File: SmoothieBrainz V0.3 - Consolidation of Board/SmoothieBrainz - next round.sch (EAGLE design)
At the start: 153 parts, among them IC1 LPC1769, IC5 LD117ADT33TR, Q1 BSL207SP, Q2 12MHz, SW1 SW_TACT_4P_B, SW3 SW_TACT_4P_B, U2 HC_05, U3 USD-SOCKETUSD, X1 GMSTBV2, X14 USBPTH, X2 MSTBA2, X3 MSTBA4

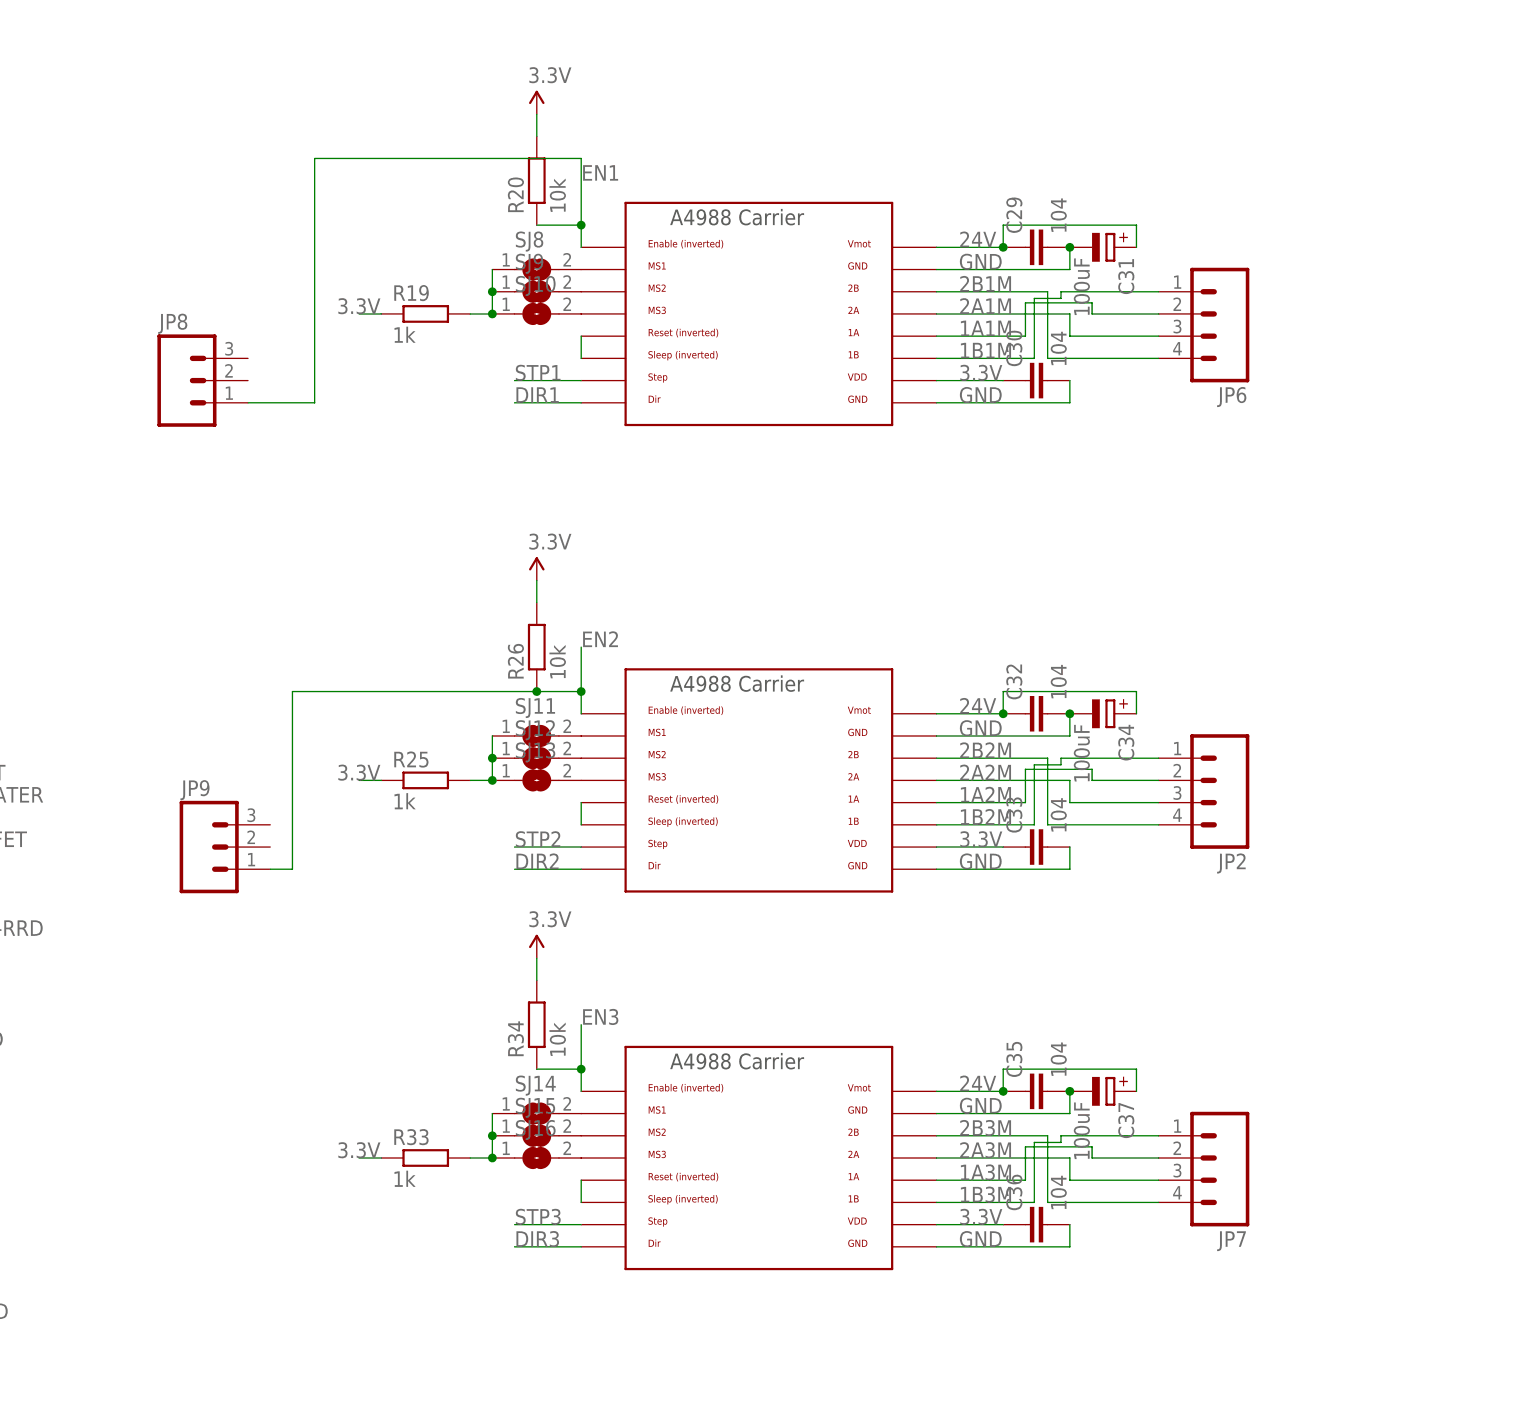
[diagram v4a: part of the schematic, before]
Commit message: about to revert y stepper layout
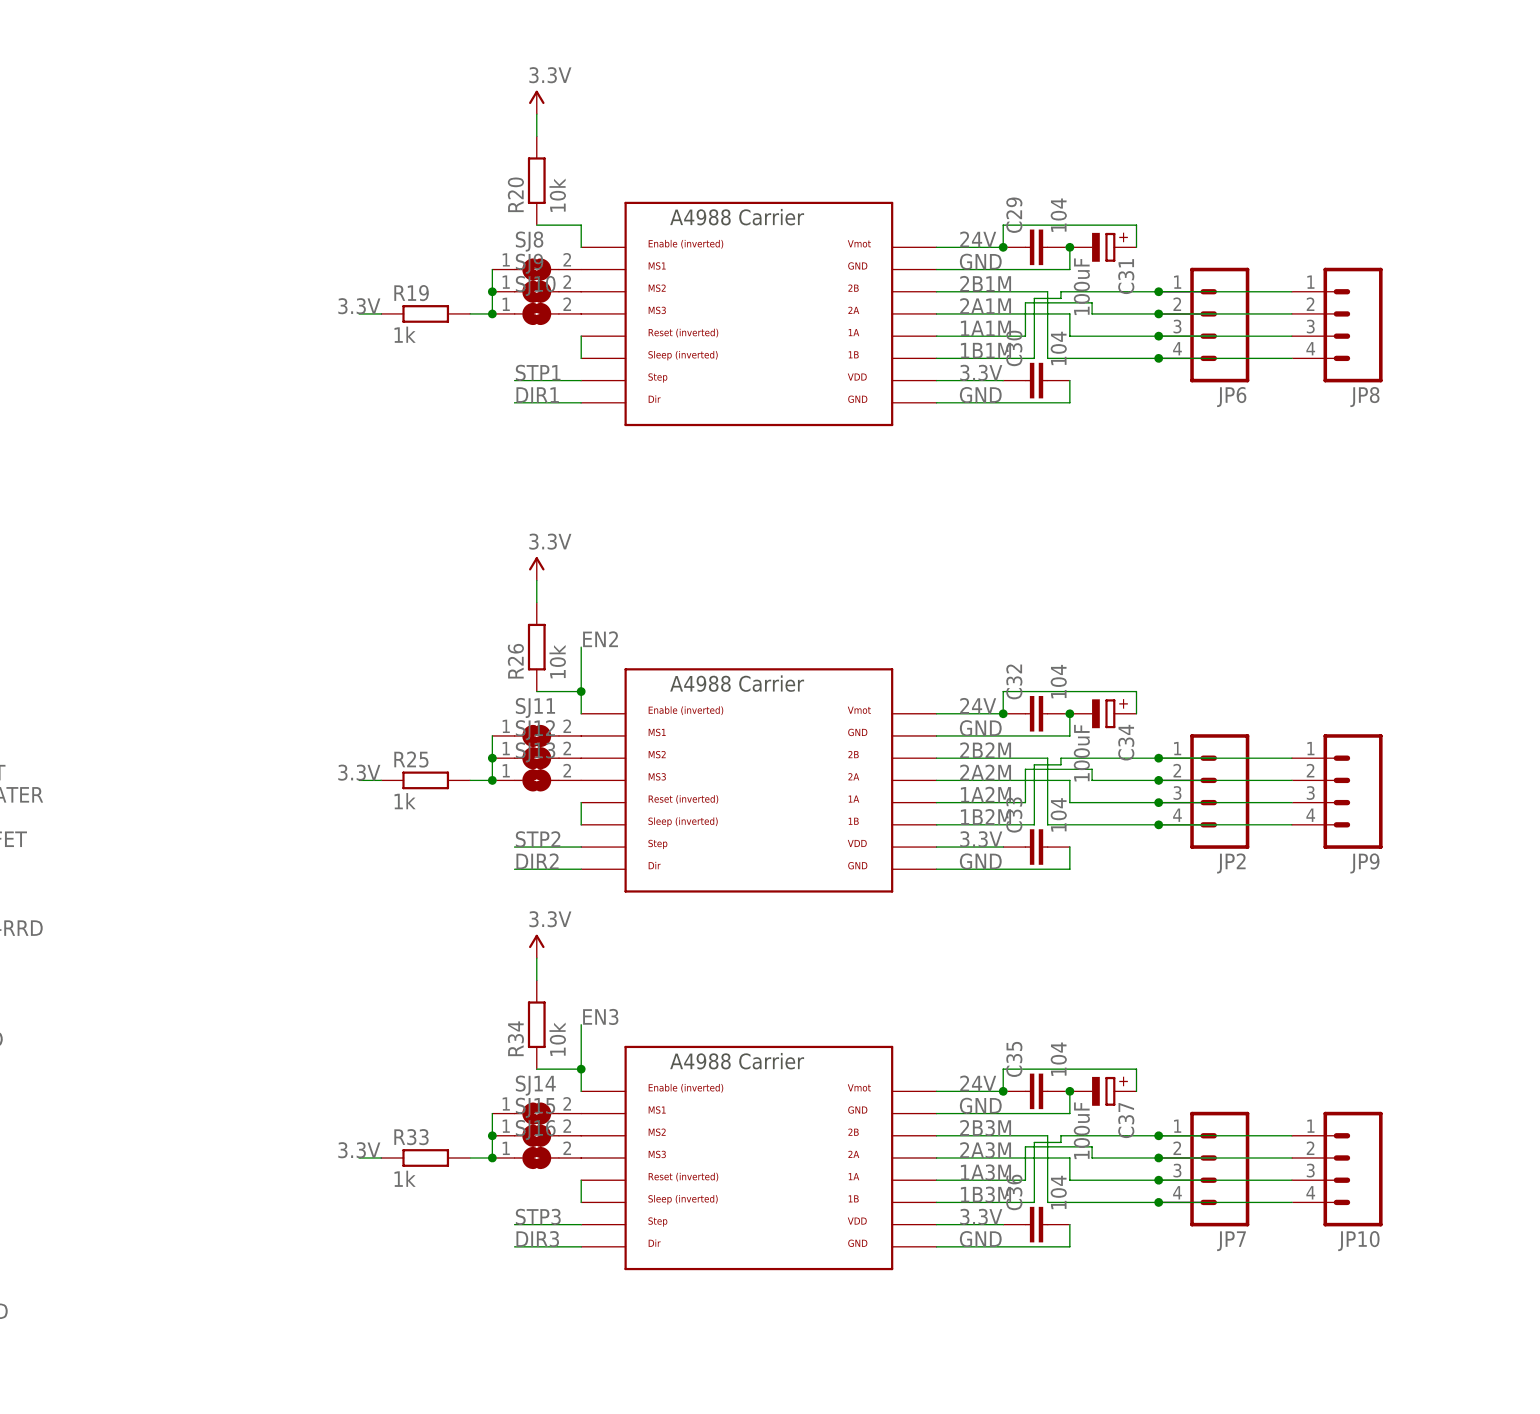
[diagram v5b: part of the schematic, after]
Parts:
- added JP10: (no value), SparkFun-Connectors:M04LOCK
- JP8, JP9: device SparkFun-Connectors:M03LOCK -> SparkFun-Connectors:M04LOCK
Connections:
- new net N$28: R20.1, U$1.EN
- net 1A1M: now also JP8.2
- net 1A2M: now also JP9.2
- net 1A3M: now also JP10.2
- net 1B1M: now also JP8.1
- net 1B2M: now also JP9.1
- net 1B3M: now also JP10.1
- net 2A1M: now also JP8.3
- net 2A2M: now also JP9.3
- net 2A3M: now also JP10.3
- net 2B1M: now also JP8.4
- net 2B2M: now also JP9.4
- net 2B3M: now also JP10.4
- net EN1: no longer JP8.1, R20.1, U$1.EN
- net EN2: no longer JP9.1
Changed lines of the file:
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@@
 <part name="R34" library="resistor" deviceset="R-EU_" device="R0603" value="10k"/>
 <part name="P+7" library="SparkFun" deviceset="3.3V" device=""/>
-<part name="JP8" library="SparkFun-Connectors" deviceset="M03" device="LOCK"/>
-<part name="JP9" library="SparkFun-Connectors" deviceset="M03" device="LOCK"/>
+<part name="JP8" library="SparkFun-Connectors" deviceset="M04" device="LOCK"/>
+<part name="JP9" library="SparkFun-Connectors" deviceset="M04" device="LOCK"/>
+<part name="JP10" library="SparkFun-Connectors" deviceset="M04" device="LOCK"/>
 </parts>
 <sheets>
@@
 <instance part="R34" gate="G$1" x="317.5" y="180.34" rot="R90"/>
 <instance part="P+7" gate="G$1" x="317.5" y="187.96"/>
-<instance part="JP8" gate="G$1" x="276.86" y="254"/>
-<instance part="JP9" gate="G$1" x="279.4" y="200.66"/>
+<instance part="JP8" gate="G$1" x="408.94" y="261.62" rot="R180"/>
+<instance part="JP9" gate="G$1" x="408.94" y="208.28" rot="R180"/>
+<instance part="JP10" gate="G$1" x="408.94" y="165.1" rot="R180"/>
 </instances>
 <busses>
@@
 <wire x1="78.74" y1="398.78" x2="106.68" y2="398.78" width="0.1524" layer="91"/>
 </segment>
-<segment>
-<pinref part="U$1" gate="G$1" pin="EN"/>
-<wire x1="322.58" y1="269.24" x2="322.58" y2="271.78" width="0.1524" layer="91"/>
-<label x="322.58" y="276.86" size="1.778" layer="95"/>
-<pinref part="R20" gate="G$1" pin="1"/>
-<wire x1="322.58" y1="271.78" x2="322.58" y2="279.4" width="0.1524" layer="91"/>
-<wire x1="317.5" y1="271.78" x2="322.58" y2="271.78" width="0.1524" layer="91"/>
-<junction x="322.58" y="271.78"/>
-<pinref part="JP8" gate="G$1" pin="1"/>
-<wire x1="284.48" y1="251.46" x2="292.1" y2="251.46" width="0.1524" layer="91"/>
-<wire x1="292.1" y1="251.46" x2="292.1" y2="279.4" width="0.1524" layer="91"/>
-<wire x1="292.1" y1="279.4" x2="322.58" y2="279.4" width="0.1524" layer="91"/>
-</segment>
 </net>
 <net name="DIR1" class="0">
@@
 <wire x1="317.5" y1="218.44" x2="322.58" y2="218.44" width="0.1524" layer="91"/>
 <junction x="322.58" y="218.44"/>
-<pinref part="JP9" gate="G$1" pin="1"/>
-<wire x1="287.02" y1="198.12" x2="289.56" y2="198.12" width="0.1524" layer="91"/>
-<wire x1="289.56" y1="198.12" x2="289.56" y2="218.44" width="0.1524" layer="91"/>
-<wire x1="289.56" y1="218.44" x2="317.5" y2="218.44" width="0.1524" layer="91"/>
-<junction x="317.5" y="218.44"/>
 </segment>
 </net>
@@
 <pinref part="JP6" gate="G$1" pin="4"/>
 <wire x1="375.92" y1="256.54" x2="388.62" y2="256.54" width="0.1524" layer="91"/>
+<pinref part="JP8" gate="G$1" pin="4"/>
+<wire x1="388.62" y1="256.54" x2="403.86" y2="256.54" width="0.1524" layer="91"/>
+<junction x="388.62" y="256.54"/>
 </segment>
 </net>
@@
 <pinref part="JP6" gate="G$1" pin="3"/>
 <wire x1="378.46" y1="259.08" x2="388.62" y2="259.08" width="0.1524" layer="91"/>
+<pinref part="JP8" gate="G$1" pin="3"/>
+<wire x1="388.62" y1="259.08" x2="403.86" y2="259.08" width="0.1524" layer="91"/>
+<junction x="388.62" y="259.08"/>
 </segment>
 </net>
@@
 <wire x1="381" y1="261.62" x2="381" y2="262.89" width="0.1524" layer="91"/>
 <wire x1="381" y1="262.89" x2="373.38" y2="262.89" width="0.1524" layer="91"/>
+<pinref part="JP8" gate="G$1" pin="2"/>
+<wire x1="388.62" y1="261.62" x2="403.86" y2="261.62" width="0.1524" layer="91"/>
+<junction x="388.62" y="261.62"/>
 </segment>
 </net>
@@
 <wire x1="377.444" y1="264.16" x2="377.444" y2="263.398" width="0.1524" layer="91"/>
 <wire x1="377.444" y1="263.398" x2="374.396" y2="263.398" width="0.1524" layer="91"/>
+<pinref part="JP8" gate="G$1" pin="1"/>
+<wire x1="388.62" y1="264.16" x2="403.86" y2="264.16" width="0.1524" layer="91"/>
+<junction x="388.62" y="264.16"/>
 </segment>
 </net>
@@
 <pinref part="JP2" gate="G$1" pin="4"/>
 <wire x1="375.92" y1="203.2" x2="388.62" y2="203.2" width="0.1524" layer="91"/>
+<pinref part="JP9" gate="G$1" pin="4"/>
+<wire x1="388.62" y1="203.2" x2="403.86" y2="203.2" width="0.1524" layer="91"/>
+<junction x="388.62" y="203.2"/>
 </segment>
 </net>
@@
 <pinref part="JP2" gate="G$1" pin="3"/>
 <wire x1="378.46" y1="205.74" x2="388.62" y2="205.74" width="0.1524" layer="91"/>
+<pinref part="JP9" gate="G$1" pin="3"/>
+<wire x1="388.62" y1="205.74" x2="403.86" y2="205.74" width="0.1524" layer="91"/>
+<junction x="388.62" y="205.74"/>
 </segment>
 </net>
@@
 <wire x1="381" y1="208.28" x2="381" y2="209.55" width="0.1524" layer="91"/>
 <wire x1="381" y1="209.55" x2="373.38" y2="209.55" width="0.1524" layer="91"/>
+<pinref part="JP9" gate="G$1" pin="2"/>
+<wire x1="388.62" y1="208.28" x2="403.86" y2="208.28" width="0.1524" layer="91"/>
+<junction x="388.62" y="208.28"/>
 </segment>
 </net>
@@
 <wire x1="377.444" y1="210.82" x2="377.444" y2="210.058" width="0.1524" layer="91"/>
 <wire x1="377.444" y1="210.058" x2="374.396" y2="210.058" width="0.1524" layer="91"/>
+<pinref part="JP9" gate="G$1" pin="1"/>
+<wire x1="388.62" y1="210.82" x2="403.86" y2="210.82" width="0.1524" layer="91"/>
+<junction x="388.62" y="210.82"/>
 </segment>
 </net>
@@
 <pinref part="JP7" gate="G$1" pin="4"/>
 <wire x1="375.92" y1="160.02" x2="388.62" y2="160.02" width="0.1524" layer="91"/>
+<pinref part="JP10" gate="G$1" pin="4"/>
+<wire x1="388.62" y1="160.02" x2="403.86" y2="160.02" width="0.1524" layer="91"/>
+<junction x="388.62" y="160.02"/>
 </segment>
 </net>
@@
 <pinref part="JP7" gate="G$1" pin="3"/>
 <wire x1="378.46" y1="162.56" x2="388.62" y2="162.56" width="0.1524" layer="91"/>
+<pinref part="JP10" gate="G$1" pin="3"/>
+<wire x1="388.62" y1="162.56" x2="403.86" y2="162.56" width="0.1524" layer="91"/>
+<junction x="388.62" y="162.56"/>
 </segment>
 </net>
@@
 <wire x1="381" y1="165.1" x2="381" y2="166.37" width="0.1524" layer="91"/>
 <wire x1="381" y1="166.37" x2="373.38" y2="166.37" width="0.1524" layer="91"/>
+<pinref part="JP10" gate="G$1" pin="2"/>
+<wire x1="388.62" y1="165.1" x2="403.86" y2="165.1" width="0.1524" layer="91"/>
+<junction x="388.62" y="165.1"/>
 </segment>
 </net>
@@
 <wire x1="377.444" y1="167.64" x2="377.444" y2="166.878" width="0.1524" layer="91"/>
 <wire x1="377.444" y1="166.878" x2="374.396" y2="166.878" width="0.1524" layer="91"/>
+<pinref part="JP10" gate="G$1" pin="1"/>
+<wire x1="388.62" y1="167.64" x2="403.86" y2="167.64" width="0.1524" layer="91"/>
+<junction x="388.62" y="167.64"/>
 </segment>
 </net>
@@
 </segment>
 </net>
+<net name="N$28" class="0">
+<segment>
+<pinref part="U$1" gate="G$1" pin="EN"/>
+<wire x1="322.58" y1="269.24" x2="322.58" y2="271.78" width="0.1524" layer="91"/>
+<pinref part="R20" gate="G$1" pin="1"/>
+<wire x1="317.5" y1="271.78" x2="322.58" y2="271.78" width="0.1524" layer="91"/>
+</segment>
+</net>

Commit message: 3rd motor wired
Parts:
- added U$11, U$12: FIDUCIAL, adafruit:FIDUCIAL
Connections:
- removed net +12VHEATBED: LED6.A
- net HEATBEDVIN: now also LED6.A
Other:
- note added: "Fiducials"
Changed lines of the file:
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@@
 <part name="JP9" library="SparkFun-Connectors" deviceset="M04" device="LOCK"/>
 <part name="JP10" library="SparkFun-Connectors" deviceset="M04" device="LOCK"/>
+<part name="U$11" library="adafruit" deviceset="FIDUCIAL" device=""/>
+<part name="U$12" library="adafruit" deviceset="FIDUCIAL" device=""/>
 </parts>
 <sheets>
@@
 cut a BOM line item</text>
 <text x="129.54" y="409.702" size="6.4516" layer="95">Thermistors</text>
+<text x="15.24" y="220.98" size="2.54" layer="95">Fiducials</text>
 </plain>
 <instances>
@@
 <instance part="JP9" gate="G$1" x="408.94" y="208.28" rot="R180"/>
 <instance part="JP10" gate="G$1" x="408.94" y="165.1" rot="R180"/>
+<instance part="U$11" gate="G$1" x="17.78" y="215.9"/>
+<instance part="U$12" gate="G$1" x="27.94" y="215.9"/>
 </instances>
 <busses>
@@
 </segment>
 </net>
-<net name="+12VHEATBED" class="4">
-<segment>
-<wire x1="500.38" y1="363.22" x2="485.14" y2="363.22" width="0.1524" layer="91"/>
-<label x="485.14" y="363.22" size="1.778" layer="95"/>
-</segment>
-<segment>
-<label x="487.68" y="378.46" size="1.778" layer="95"/>
-<pinref part="LED6" gate="G$1" pin="A"/>
-<wire x1="508" y1="378.46" x2="485.14" y2="378.46" width="0.1524" layer="91"/>
-</segment>
-</net>
 <net name="HEATBED-CONTROL" class="0">
 <segment>
@@
 <label x="78.74" y="276.86" size="1.778" layer="95"/>
 </segment>
+<segment>
+<wire x1="500.38" y1="363.22" x2="485.14" y2="363.22" width="0.1524" layer="91"/>
+<label x="485.14" y="363.22" size="1.778" layer="95"/>
+</segment>
+<segment>
+<label x="487.68" y="378.46" size="1.778" layer="95"/>
+<pinref part="LED6" gate="G$1" pin="A"/>
+<wire x1="508" y1="378.46" x2="485.14" y2="378.46" width="0.1524" layer="91"/>
+</segment>
 </net>
